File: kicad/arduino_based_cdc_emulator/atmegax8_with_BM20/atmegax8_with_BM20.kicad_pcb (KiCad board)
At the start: 2 copper layers, 50 x 50 mm, 70 parts, among them IC1 ATMEGA88-A, P1 CONN_9, P2 SPI, P3 CONN_4, Q1 BC817-40, U1 78L05, U2 F-6188, U3 LM358, Y1 Crystal_GND2

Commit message: update
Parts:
- removed C11: 47m/25V, Capacitors_Tantalum_SMD:TantalC_SizeD_EIA-7343_HandSoldering
- removed C12, C8: 100n, Capacitors_SMD:C_0805_HandSoldering
- removed C15, C16, C17: 33p, Capacitors_SMD:C_0805_HandSoldering
- removed C19: 10m/16V, Capacitors_SMD:CP_Elec_5x5.8
- removed C20: 10m/16V, Capacitors_SMD:c_elec_5x5.8
- removed C26: 10n, Capacitors_SMD:C_0805_HandSoldering
- removed L1: 330u, SMD_Packages:SMD-1210_Pol
- removed P2: SPI, Pin_Headers:Pin_Header_Straight_2x03
- removed P3: CONN_4, Pin_Headers.pretty:Pin_Header_Straight_1x04
- removed Q1: BC817-40, TO_SOT_Packages_SMD:SOT-23
- added C1: 100n, Capacitors_SMD.pretty:C_0805_HandSoldering, B.Cu at (-40.3, 70.8)
- added C2: 100n, Capacitors_SMD.pretty:C_0805_HandSoldering, F.Cu at (-21.4, 56.1)
- added J1: TEST_FLASH_MODE, Pin_Headers:Pin_Header_Straight_2x02_Pitch2.54mm, B.Cu at (-16.6, 47.6)
- added JP1: Jumper_3_Bridged12, Jumper:SolderJumper-3_P1.3mm_Open_RoundedPad1.0x1.5mm_NumberLabels, F.Cu at (-33.7, 49.4)
- added R32: NP, Resistors_SMD:R_0805_HandSoldering, F.Cu at (-17.3, 54.6)
- added R33: 4k7, Resistors_SMD:R_0805_HandSoldering, F.Cu at (-20.9, 45.5)
- added R34: 4k7, Resistors_SMD:R_0805_HandSoldering, B.Cu at (-26.6, 66.5)
- added R35: 4k7, Resistors_SMD:R_0805_HandSoldering, F.Cu at (-20.9, 48.1)
- C10: value 100m/25V -> CTS 47u/25V D 10% VIS-293D; footprint Capacitors_SMD:c_elec_6.3x7.7 -> Capacitors_Tantalum_SMD.pretty:TantalC_SizeD_EIA-7343_HandSoldering; moved to F.Cu
- C13: footprint Capacitors_Tantalum_SMD:TantalC_SizeA_EIA-3216_HandSoldering -> Capacitors_Tantalum_SMD.pretty:TantalC_SizeA_EIA-3216_HandSoldering
- C14: value 47m/25V -> 4u7/25V; footprint Capacitors_SMD:c_elec_6.3x5.7 -> Capacitors_SMD.pretty:c_elec_5x5.8
- C18: value 33p -> 10n; footprint Capacitors_SMD:C_0805_HandSoldering -> Capacitors_SMD.pretty:C_0805_HandSoldering
- C21: value 10m/16V -> 4m7/16V; footprint Capacitors_SMD:c_elec_5x5.8 -> Capacitors_SMD.pretty:c_elec_5x5.8
- C22: value 4u7/10V -> 2u2/16V; footprint Capacitors_SMD:C_1206_HandSoldering -> Capacitors_Tantalum_SMD.pretty:TantalC_SizeA_EIA-3216_HandSoldering
- C23: footprint Capacitors_SMD:C_0805_HandSoldering -> Capacitors_SMD.pretty:C_1206_HandSoldering; moved to F.Cu
- C24: footprint Capacitors_Tantalum_SMD:TantalC_SizeA_EIA-3216_HandSoldering -> Capacitors_Tantalum_SMD.pretty:TantalC_SizeA_EIA-3216_HandSoldering; moved to B.Cu
- C25: value 2u1 -> 2u2; footprint Capacitors_Tantalum_SMD:TantalC_SizeA_EIA-3216_HandSoldering -> Capacitors_Tantalum_SMD.pretty:TantalC_SizeA_EIA-3216_HandSoldering
- C27: footprint Capacitors_SMD:C_0805_HandSoldering -> Capacitors_SMD.pretty:C_1206_HandSoldering
- C28: value 100n -> 2u2/16V; footprint Capacitors_SMD:C_0805_HandSoldering -> Capacitors_Tantalum_SMD.pretty:TantalC_SizeA_EIA-3216_HandSoldering
- C3: value 100n -> 10m/16V; footprint Capacitors_SMD:C_0805_HandSoldering -> Capacitors_Tantalum_SMD.pretty:TantalC_SizeB_EIA-3528_HandSoldering
- C4: value 100n -> 10n; footprint Capacitors_SMD:C_0805_HandSoldering -> Capacitors_SMD.pretty:C_0805_HandSoldering
- C5: value 100n -> 4m7/16V; footprint Capacitors_SMD:C_0805_HandSoldering -> Capacitors_SMD.pretty:c_elec_5x5.8
- C6: value 10m/16V -> 100n; footprint Capacitors_SMD:c_elec_5x5.8 -> Capacitors_SMD.pretty:C_0805_HandSoldering; moved to F.Cu
- C7: footprint Capacitors_SMD:C_0805_HandSoldering -> Capacitors_SMD.pretty:C_0805_HandSoldering; moved to B.Cu
- C9: footprint Capacitors_SMD:c_elec_6.3x5.7 -> Capacitors_SMD.pretty:c_elec_5x5.8
- D1: value 1N4148 -> 5V1; footprint Diodes_SMD:MiniMELF_Handsoldering -> Diodes_SMD.pretty:MiniMELF_Handsoldering; moved to F.Cu
- IC1: footprint Housings_QFP:TQFP-32_7x7mm_Pitch0.8mm -> Housings_QFP.pretty:LQFP-32_7x7mm_Pitch0.8mm
- P1: value CONN_9 -> CONN_10; footprint Pin_Headers:Pin_Header_Straight_1x11 -> Pin_Headers:Pin_Header_Straight_1x12_Pitch2.54mm; moved to F.Cu
- R10: value 39R -> 100k
- R11, R12, R24, R28: value 47k -> 100k
- R13, R7: moved to B.Cu
- R15, R18: value 47k -> 2M2; moved to F.Cu
- R20: value 22k -> 560; moved to F.Cu
- R21: value 22k -> NP; moved to F.Cu
- R22: value 47k -> 1k
- R23: value 22k -> 820; moved to F.Cu
- R25: value 1k2 -> 2k
- R26: value 1k -> 100k; moved to F.Cu
- R27: value 1k2 -> 1k; moved to F.Cu
- R30: value 10k -> 820
- R31: value 1k -> 560; moved to F.Cu
- R8: value 22k -> 330; moved to F.Cu
- R9: value 39R -> 330
- U1: value 78L05 -> 78L05-RESCUE-atmegax8_with_BM20; footprint my_modules:SOT-223-REGULATOR -> modules:SOT-223-REGULATOR; moved to B.Cu
- U2: value F-6188 -> BM20; footprint modules:F-6188_nosilk -> bluetooth:BM20
- Y1: value Crystal_GND2 -> Crystal_GND24; footprint modules:MURATA_CSTCE_V53 -> Crystals.pretty:crystal_FA238-TSX3225
- moved D2 148.6 mm to (-39.4, 55.7), turned to 180 degrees
- moved D3 146.0 mm to (-39.4, 53.5), turned to 180 degrees
- moved D1 142.6 mm to (-40.2, 48.8), turned to 90 degrees
- moved R13 141.6 mm to (-39.3, 50.9)
- moved C10 140.5 mm to (-40.9, 65.5), turned to 270 degrees
- moved R29 139.7 mm to (-36.0, 53.8), turned to 180 degrees
- moved C25 137.6 mm to (-29.1, 48.1)
- moved R19 136.5 mm to (-32.8, 45.4), turned to 180 degrees
- moved R4 134.0 mm to (-36.1, 49.3)
- moved R14 133.9 mm to (-31.3, 49.3), turned to 90 degrees
- moved U1 133.8 mm to (-40.2, 64.0)
- moved R1 133.3 mm to (-36.0, 56.1), turned to 0 degrees
- moved C24 132.8 mm to (-32.2, 67.9), turned to 180 degrees
- moved R3 132.5 mm to (-26.8, 49.3), turned to 90 degrees
- moved R5 131.6 mm to (-35.9, 63.5), turned to 0 degrees
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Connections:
- C13 pad 2: GNDA -> GND
- C18 pad 2: /VGND -> GNDA
- C21 pad 2: /BTOUTLN -> /BTOUTL
- C28 pad 1: /MIC_BIAS -> Net-(C28-Pad1)
- C3 pad 1: +12V -> Net-(C3-Pad1)
- C4 pad 1: +5V -> Net-(C4-Pad1)
- C4 pad 2: GND -> GNDA
- C5 pad 1: +BATT -> Net-(C5-Pad1)
- C5 pad 2: GND -> /BTOUTR
- C6 pad 1: /BTOUTL -> +5V
- C6 pad 2: Net-(C6-Pad2) -> GND
- C7 pad 1: Net-(C7-Pad1) -> +5V
- C7 pad 2: GNDA -> GND
- D1 pad 1: +BATT -> /CDC_ENA_5V
- D1 pad 2: +5V -> GND
- D2 pad 1: GND -> /LED1
- D2 pad 2: Net-(D2-Pad2) -> /SYSPWR
- D3 pad 1: GND -> /LED2
- D3 pad 2: Net-(D3-Pad2) -> /SYSPWR
- IC1 pad 10: (no net) -> Net-(IC1-Pad10)
- IC1 pad 12: (no net) -> Net-(IC1-Pad12)
- IC1 pad 15: /MOSI -> (no net)
- IC1 pad 16: /MISO -> (no net)
- IC1 pad 17: /SCK -> (no net)
- IC1 pad 9: (no net) -> Net-(IC1-Pad9)
- P1 pad 10: /CDC_ENA_12V -> /DataOut
- P1 pad 11: Net-(P1-Pad11) -> /CDC_ENA_12V
- P1 pad 4: /MIC_IN2 -> GNDA
- P1 pad 5: /MIC_IN1 -> /MIC_IN2
- P1 pad 6: +12V -> /MIC_IN1
- P1 pad 7: GND -> +12V
- P1 pad 8: Net-(P1-Pad8) -> GND
- P1 pad 9: /DataOut -> Net-(P1-Pad9)
- R1 pad 1: Net-(P1-Pad8) -> Net-(P1-Pad9)
- R10 pad 1: Net-(C8-Pad1) -> /VGND
- R10 pad 2: /AOUTL -> Net-(R10-Pad2)
- R13 pad 2: RX -> /RX
- R14 pad 2: TX -> /TX
- R15 pad 1: Net-(C15-Pad2) -> Net-(R15-Pad1)
- R16 pad 2: +12C -> +12V
- R17 pad 1: GNDA -> GND
- R18 pad 1: Net-(C16-Pad2) -> Net-(R10-Pad2)
- R19 pad 1: TX -> /TX
- R2 pad 1: Net-(P1-Pad11) -> Net-(P1-Pad12)
- R20 pad 1: Net-(C19-Pad1) -> GNDA
- R20 pad 2: Net-(C17-Pad1) -> Net-(C21-Pad1)
- R21 pad 1: Net-(C15-Pad2) -> GNDA
- R21 pad 2: Net-(C20-Pad2) -> /BTOUTL
- R22 pad 1: /VGND -> Net-(C28-Pad1)
- R22 pad 2: Net-(C17-Pad1) -> /MIC_BIAS
- R26 pad 1: /LED1 -> /VGND
- R26 pad 2: Net-(D2-Pad2) -> Net-(R15-Pad1)
- R27 pad 2: /MIC_BIAS -> Net-(C28-Pad1)
- R28 pad 1: Net-(Q1-Pad1) -> /VGND
- R28 pad 2: GND -> Net-(C4-Pad1)
- R29 pad 1: Net-(Q1-Pad1) -> /CDC_ENA_5V
- R30 pad 1: +5V -> Net-(C5-Pad1)
- R30 pad 2: /CDC_ENA_5V -> Net-(C4-Pad1)
- R31 pad 1: /LED2 -> GNDA
- R31 pad 2: Net-(D3-Pad2) -> Net-(C5-Pad1)
- R4 pad 1: Net-(IC1-Pad32) -> Net-(JP1-Pad2)
- R7 pad 2: +BATT -> +5V
- R8 pad 1: Net-(C16-Pad2) -> Net-(IC1-Pad9)
- R8 pad 2: Net-(C6-Pad2) -> /BT_RESET
- R9 pad 1: Net-(C7-Pad1) -> Net-(IC1-Pad10)
- R9 pad 2: /AOUTR -> /MFB
- U2 pad 1: GND -> (no net)
- U2 pad 10: TX -> Net-(C3-Pad1)
- U2 pad 11: RX -> /MICP
- U2 pad 12: (no net) -> /MICN
- U2 pad 13: /LED1 -> /MIC_BIAS
- U2 pad 14: /LED2 -> (no net)
- U2 pad 16: GND -> /BT_RESET
- U2 pad 17: GND -> (no net)
- U2 pad 18: /IN_DETECT -> (no net)
- U2 pad 19: /INR -> (no net)
- U2 pad 20: /INL -> +5V
- U2 pad 21: /MICN -> (no net)
- U2 pad 22: /MICP -> (no net)
- U2 pad 23: /MIC_BIAS -> GND
- U2 pad 24: /BTOUTLN -> /SYSPWR
- U2 pad 25: /BTOUTL -> (no net)
- U2 pad 26: /BTOUTR -> /MFB
- U2 pad 27: /BTOUTRN -> /LED1
- U2 pad 28: (no net) -> /LED2
- U2 pad 29: +BATT -> (no net)
- U2 pad 3: GND -> (no net)
- U2 pad 32: GND -> /RX
- U2 pad 4: (no net) -> /P2_0
- U2 pad 7: (no net) -> /BTOUTR
- U2 pad 8: /BT_RESET -> GNDA
- U2 pad 9: (no net) -> /BTOUTL
- U3 pad 2: Net-(C16-Pad2) -> Net-(R10-Pad2)
- U3 pad 5: Net-(C17-Pad1) -> Net-(C4-Pad1)
- U3 pad 6: Net-(C15-Pad2) -> Net-(R15-Pad1)
- U3 pad 8: +12C -> +12V
- Y1 pad 2: GND -> Net-(IC1-Pad7)
- Y1 pad 3: Net-(IC1-Pad7) -> GND
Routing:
- net GND: track 106.1 -> 29.1 mm, vias 4 -> 3
- net +BATT: track 60.1 -> 0.00 mm, vias 2 -> 0
- net GNDA: track 58.8 -> 0.00 mm, vias 1 -> 0
- net /MIC_BIAS: track 43.7 -> 0.00 mm
- net /BTOUTRN: track 39.8 -> 0.00 mm, vias 2 -> 0
- net /MICN: track 39.3 -> 0.00 mm, vias 3 -> 0
- net /AOUTL: track 38.9 -> 0.00 mm
- net /MICP: track 44.9 -> 6.20 mm, vias 2 -> 1
- net +5V: track 70.5 -> 34.1 mm, vias 5 -> 2
- net /BTOUTR: track 34.5 -> 0.00 mm, vias 2 -> 0
- net +12V: track 28.7 -> 0.00 mm
- net /BTOUTL: track 27.4 -> 0.00 mm, vias 2 -> 0
- net +12C: track 26.8 -> 0.00 mm, vias 1 -> 0
- net /BTOUTLN: track 26.2 -> 0.00 mm, vias 2 -> 0
- net /ARESET: track 31.2 -> 6.13 mm, vias 2 -> 0
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- removed copper zone on B.Cu, net GND
- removed copper zone on B.Cu, net GNDA
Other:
- board outline removed
- net class Default: clearance 0.2 -> 0.15; trace_width 0.3 -> 0.15; via_dia 0.8 -> 0.5; via_drill 0.5 -> 0.3
- rule trace_clearance: 0.2 -> 0.15
- rule trace_min: 0.2032 -> 0.127
- rule via_min_drill: 0.5 -> 0.2
- rule via_min_size: 0.5 -> 0.45

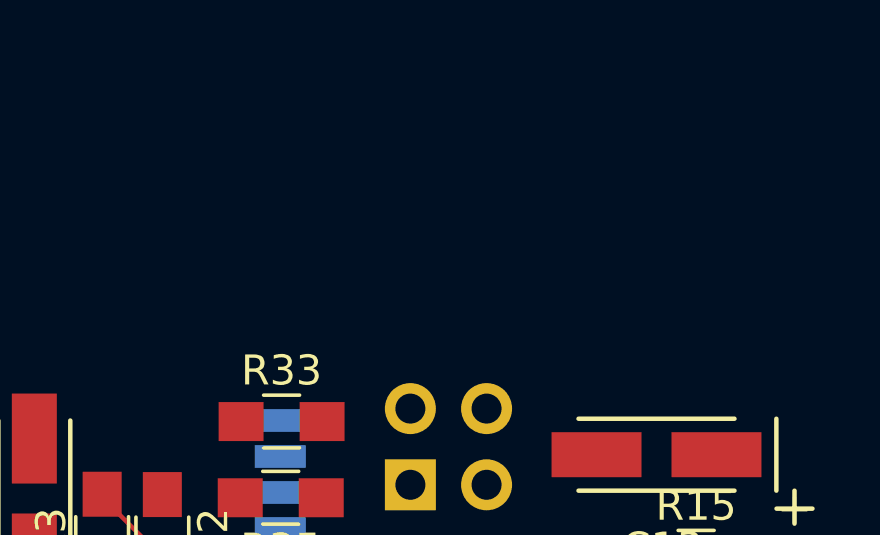
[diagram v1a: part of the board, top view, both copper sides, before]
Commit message: changes to BM20 version, not finished yet
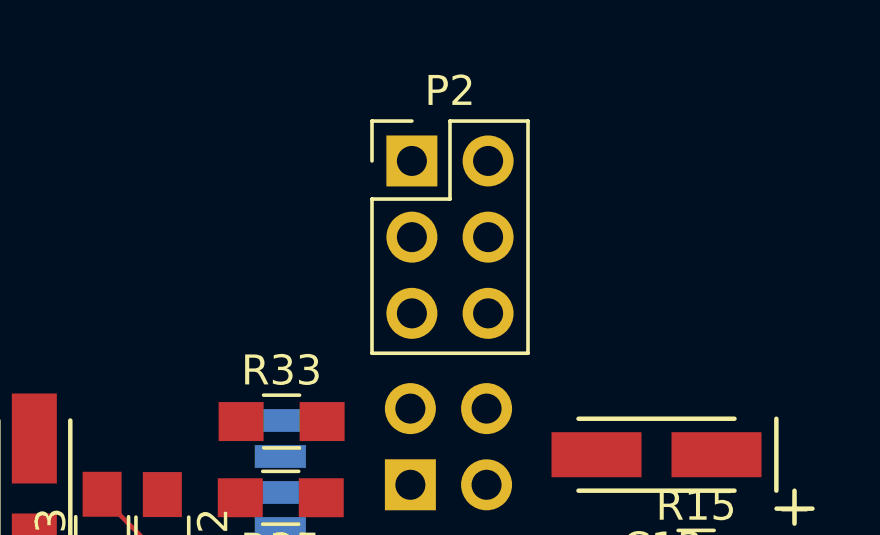
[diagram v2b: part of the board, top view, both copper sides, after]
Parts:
- added P2: SPI, Pin_Headers:Pin_Header_Straight_2x03_Pitch2.54mm, F.Cu at (-16.5, 36.8)
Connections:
- IC1 pad 15: (no net) -> /MOSI
- IC1 pad 16: (no net) -> /MISO
- IC1 pad 17: (no net) -> /SCK
